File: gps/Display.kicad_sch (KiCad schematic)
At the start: 14 parts, among them U4 HT16k33, U5 7seg_1x1_rgb, U6 7seg_1x1_rgb, U7 7seg_1x1_rgb, U8 CA56-12CGKWA

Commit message: update pcd/sch
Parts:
- U8: footprint Display_7Segment:CA56-12CGKWA -> 7seg_rgb:7seg_4x1
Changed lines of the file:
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@@
 			)
 		)
-		(property "Footprint" "Display_7Segment:CA56-12CGKWA"
+		(property "Footprint" "7seg_rgb:7seg_4x1"
 			(at 128.27 114.3 0)
 			(effects

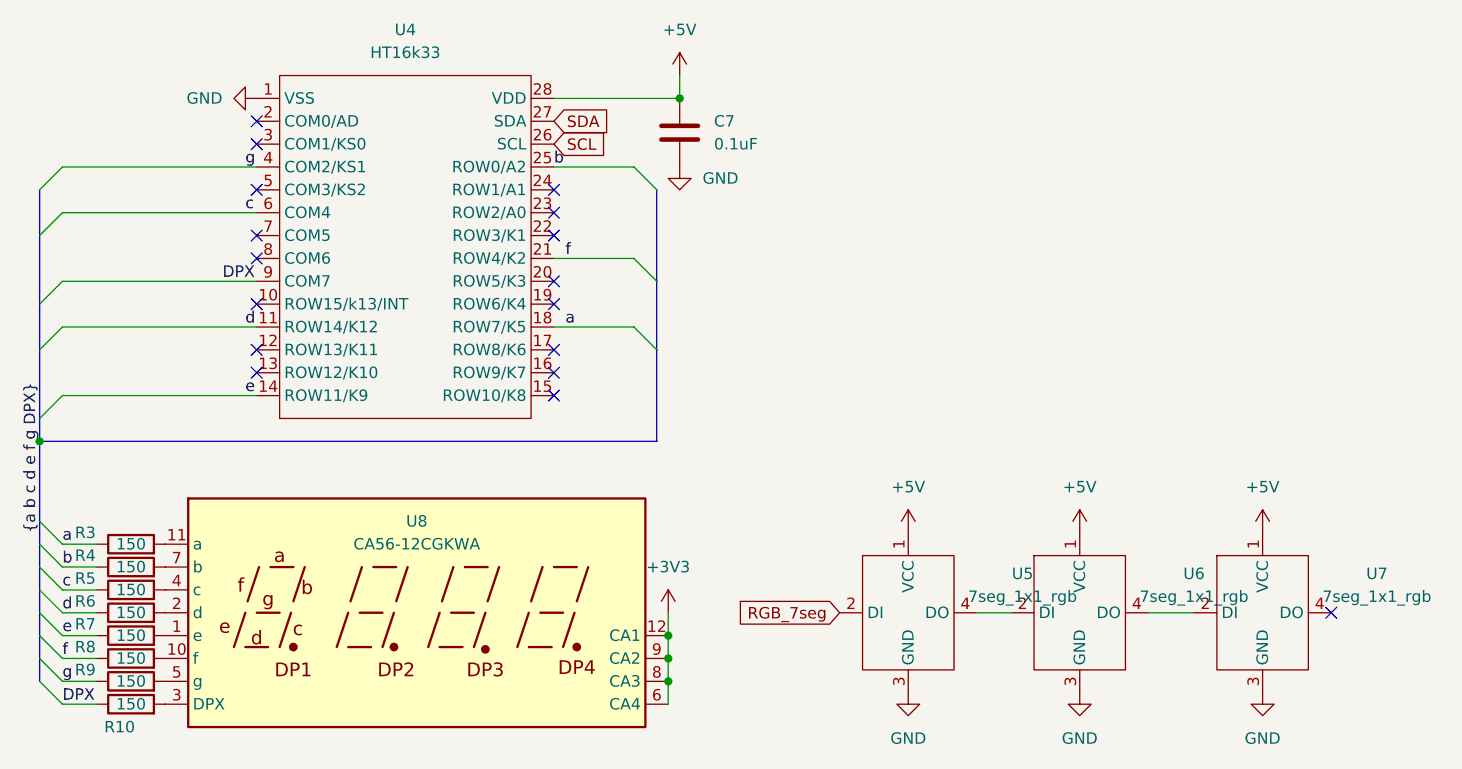
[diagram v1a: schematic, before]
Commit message: update pcd/sch
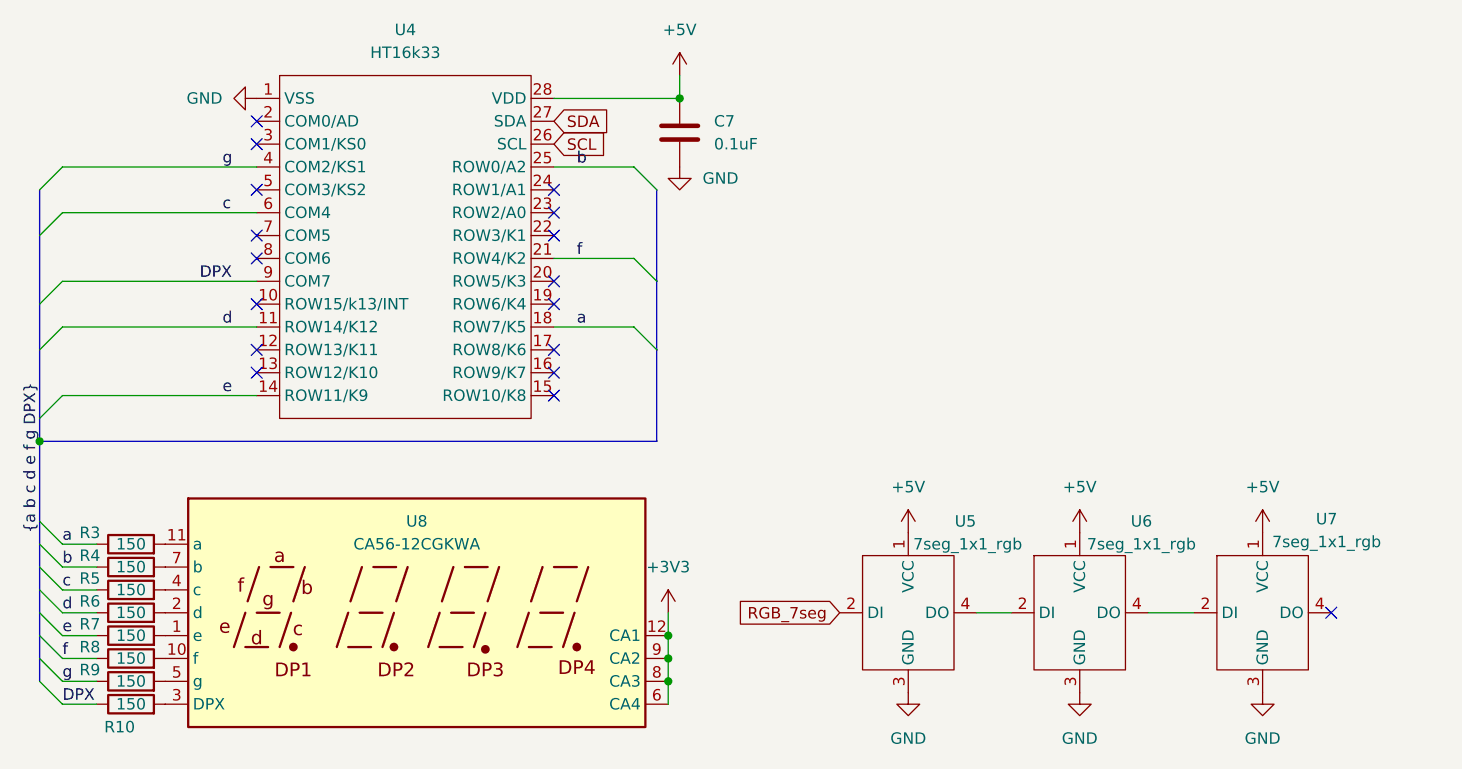
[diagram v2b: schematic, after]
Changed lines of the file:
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@@
+		)
+	)
+	(wire
+		(pts
+			(xy 143.51 49.53) (xy 152.4 49.53)
+		)
+		(stroke
+			(width 0)
+			(type default)
 		)
 	)
@@
 	(wire
 		(pts
-			(xy 152.4 49.53) (xy 143.51 49.53)
+			(xy 143.51 59.69) (xy 152.4 59.69)
 		)
 		(stroke
@@
 	(wire
 		(pts
-			(xy 143.51 59.69) (xy 152.4 59.69)
-		)
-		(stroke
-			(width 0)
-			(type default)
-		)
-	)
-	(wire
-		(pts
 			(xy 156.21 101.6) (xy 156.21 104.14)
 		)
@@
 	)
 	(label "DPX"
-		(at 106.68 62.23 0)
+		(at 104.14 62.23 0)
 		(fields_autoplaced yes)
 		(effects
@@
 	)
 	(label "e"
-		(at 109.22 74.93 0)
+		(at 106.68 74.93 0)
 		(fields_autoplaced yes)
 		(effects
@@
 	)
 	(label "a"
-		(at 144.78 67.31 0)
+		(at 146.05 67.31 0)
 		(fields_autoplaced yes)
 		(effects
@@
 	)
 	(label "g"
-		(at 109.22 49.53 0)
+		(at 106.68 49.53 0)
 		(fields_autoplaced yes)
 		(effects
@@
 	)
 	(label "d"
-		(at 109.22 67.31 0)
+		(at 106.68 67.31 0)
 		(fields_autoplaced yes)
 		(effects
@@
 	)
 	(label "f"
-		(at 144.78 59.69 0)
+		(at 146.05 59.69 0)
 		(fields_autoplaced yes)
 		(effects
@@
 	)
 	(label "b"
-		(at 143.51 49.53 0)
+		(at 146.05 49.53 0)
 		(fields_autoplaced yes)
 		(effects
@@
 	)
 	(label "c"
-		(at 109.22 54.61 0)
+		(at 106.68 54.61 0)
 		(fields_autoplaced yes)
 		(effects
@@
 		(dnp no)
 		(property "Reference" "R9"
-			(at 91.44 105.41 90)
+			(at 91.948 105.41 90)
 			(effects
 				(font
@@
 		(dnp no)
 		(property "Reference" "R6"
-			(at 91.44 97.79 90)
+			(at 91.948 97.79 90)
 			(effects
 				(font
@@
 		(dnp no)
 		(property "Reference" "R7"
-			(at 91.44 100.33 90)
+			(at 91.948 100.33 90)
 			(effects
 				(font
@@
 		(dnp no)
 		(property "Reference" "R5"
-			(at 91.44 95.25 90)
+			(at 91.948 95.25 90)
 			(effects
 				(font
@@
 		(dnp no)
 		(property "Reference" "R8"
-			(at 91.44 102.87 90)
+			(at 91.948 102.87 90)
 			(effects
 				(font
@@
 		(on_board yes)
 		(dnp no)
-		(fields_autoplaced yes)
 		(property "Reference" "U5"
-			(at 195.58 94.7293 0)
+			(at 189.23 88.9 0)
 			(effects
 				(font
@@
 		)
 		(property "Value" "7seg_1x1_rgb"
-			(at 195.58 97.2693 0)
+			(at 189.484 91.44 0)
 			(effects
 				(font
@@
 		(on_board yes)
 		(dnp no)
-		(fields_autoplaced yes)
 		(property "Reference" "U6"
-			(at 214.63 94.7293 0)
+			(at 208.788 88.9 0)
 			(effects
 				(font
@@
 		)
 		(property "Value" "7seg_1x1_rgb"
-			(at 214.63 97.2693 0)
+			(at 208.788 91.44 0)
 			(effects
 				(font
@@
 		(dnp no)
 		(property "Reference" "R3"
-			(at 91.44 90.17 90)
+			(at 91.948 90.17 90)
 			(effects
 				(font
@@
 		(dnp no)
 		(property "Reference" "R4"
-			(at 91.44 92.71 90)
+			(at 91.948 92.71 90)
 			(effects
 				(font
@@
 		(on_board yes)
 		(dnp no)
-		(fields_autoplaced yes)
 		(property "Reference" "U7"
-			(at 234.95 94.7293 0)
+			(at 229.362 88.646 0)
 			(effects
 				(font
@@
 		)
 		(property "Value" "7seg_1x1_rgb"
-			(at 234.95 97.2693 0)
-			(effects
-				(font
+			(at 229.362 91.186 0)
+			(effects
+				(font

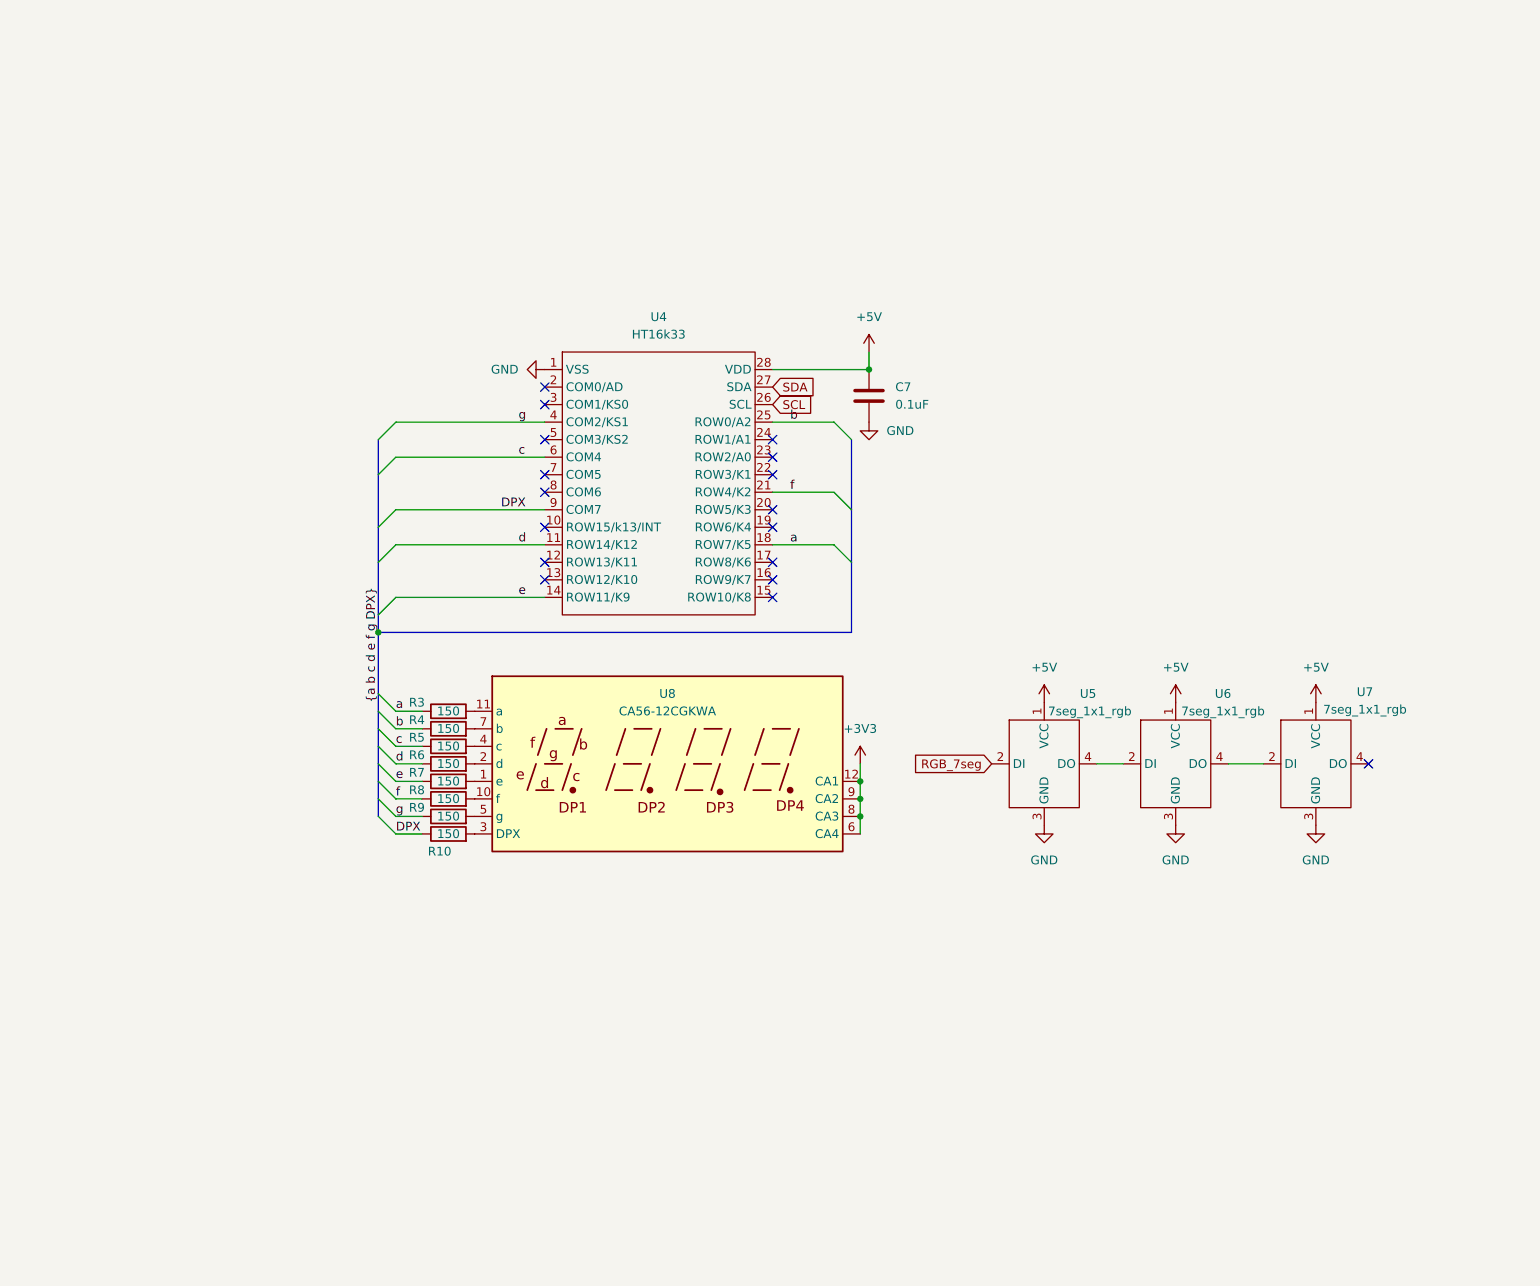
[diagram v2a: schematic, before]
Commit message: update pcb/housing
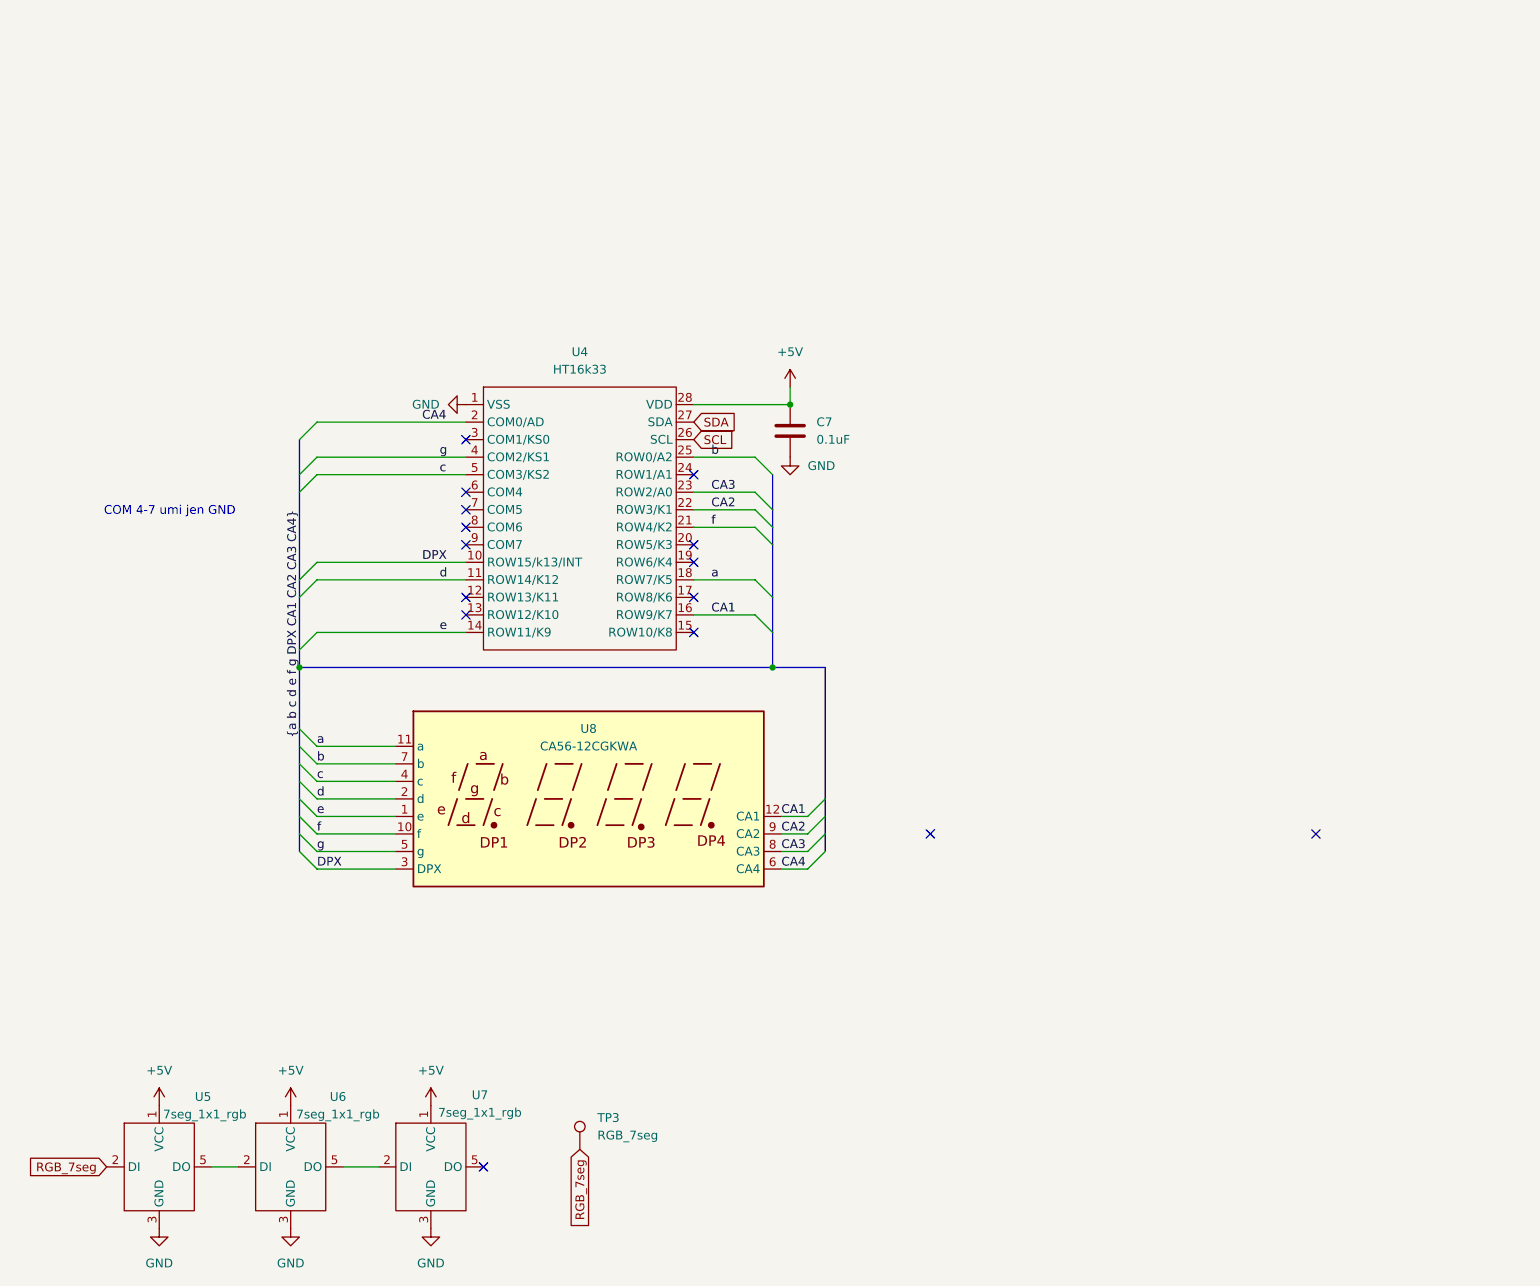
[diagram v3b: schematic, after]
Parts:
- removed R10, R3, R4, R5, R6, R7, R8, R9: 150, Resistor_SMD:R_0805_2012Metric_Pad1.20x1.40mm_HandSolder, symbol Device:R
- added TP3: RGB_7seg, TestPoint:TestPoint_Loop_D1.80mm_Drill1.0mm_Beaded, symbol Connector:TestPoint
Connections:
- net DPX: now also U4.10 (ROW15/k13/INT), U8.3 (DPX); no longer U4.9 (COM7)
- net RGB_7seg: now also TP3.1
- net a: now also U8.11 (a)
- net b: now also U8.7 (b)
- net c: now also U4.5 (COM3/KS2), U8.4 (c); no longer U4.6 (COM4)
- net d: now also U8.2 (d)
- net e: now also U8.1 (e)
- net f: now also U8.10 (f)
- net g: now also U8.5 (g)
- net CA1: now reaches U4.16 (ROW9/K7)
- net CA1: now also U8.12 (CA1)
- net CA4: now reaches U4.2 (COM0/AD)
- net CA4: now also U8.6 (CA4)
- net CA2: now reaches U4.22 (ROW3/K1)
- net CA2: now also U8.9 (CA2)
- net CA3: now reaches U4.23 (ROW2/A0)
- net CA3: now also U8.8 (CA3)
- net at U6.2 (DI): now also U5.5 (DO); no longer U5.4 (DO)
- net at U7.2 (DI): now also U6.5 (DO); no longer U6.4 (DO)
- removed net +3V3: U8.12 (CA1), U8.6 (CA4), U8.8 (CA3), U8.9 (CA2)
- no-connect marks 17 -> 15
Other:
- note added: "COM 4-7 umi jen GND"
- moved on the sheet: C7, U4, U5, U6, U7, U8

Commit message: update
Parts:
- added DS1: LTC-4724JF, Display_7Segment:LTC4724JF, symbol LTC-4724JF:LTC-4724JF
- C7: value 0.1uF -> 100nF; footprint Capacitor_SMD:C_0603_1608Metric_Pad1.08x0.95mm_HandSolder -> Capacitor_SMD:C_0805_2012Metric_Pad1.18x1.45mm_HandSolder
- U8: value CA56-12CGKWA -> KW4-804AGB
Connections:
- net CA4: now also U4.24 (ROW1/A1); no longer U4.2 (COM0/AD)
- net b: now also U4.4 (COM2/KS1); no longer U4.25 (ROW0/A2)
- net d: now also U4.8 (COM6); no longer U4.11 (ROW14/K12)
- net f: now also U4.3 (COM1/KS0); no longer U4.21 (ROW4/K2)
- net g: now also U4.5 (COM3/KS2); no longer U4.4 (COM2/KS1)
- net aBL2: now reaches U4.12 (ROW13/K11)
- net aBL2: now also DS1.11 (ANODE_BL2)
- net aAL1: now reaches U4.13 (ROW12/K10)
- net aAL1: now also DS1.12 (ANODE_AL1)
- net aE: now reaches U4.15 (ROW10/K8)
- net aE: now also DS1.2 (ANODE_E)
- net aCL3: now reaches U4.17 (ROW8/K6)
- net aCL3: now also DS1.3 (ANODE_CL3)
- net aD: now reaches U4.19 (ROW6/K4)
- net aD: now also DS1.4 (ANODE_D)
- net CC2: now reaches U4.6 (COM4)
- net CC2: now also U8.4 (c), DS1.5 (COMMON_CATHODE_DIGIT_2)
- net CC1: now reaches U4.7 (COM5)
- net CC1: now also U8.3 (DPX), DS1.1 (COMMON_CATHODE_DIGIT_1)
- net L123: now reaches U4.9 (COM7)
- net L123: now also U8.1 (e), DS1.14 (COMMON_CATHODE__L1L2L3)
- net DPX: no longer names the net of U4.10 (ROW15/k13/INT)
- net DPX: no longer U8.3 (DPX)
- net a: no longer names the net of U4.18 (ROW7/K5)
- net a: no longer U8.11 (a)
- removed net c: U4.5 (COM3/KS2), U8.4 (c)
- net e renamed aDP
- net aDP: now also DS1.6 (ANODE_DP); no longer U8.1 (e)
- new net CC3: DS1.7 (COMMON_CATHODE_DIGIT_3), U4.2 (COM0/AD), U8.11 (a)
- new net aF: DS1.15 (ANODE_F), U4.11 (ROW14/K12)
- new net aG: DS1.8 (ANODE_G), U4.25 (ROW0/A2)
- no-connect marks 15 -> 5
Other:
- note added: "ROW+ anode COM- cathode"

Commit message: PCB-update
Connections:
- net aAL1: now also U4.12 (ROW13/K11); no longer U4.13 (ROW12/K10)
- net aBL2: now also U4.13 (ROW12/K10); no longer U4.12 (ROW13/K11)
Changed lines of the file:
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@@
 	(generator_version "8.0")
 	(paper "A4")
+	(bus_alias "7Seg"
+		(members "a" "b" "c" "d" "e" "f" "g" "DPX" "CA1" "CA2" "CA3" "CA4" "CC1"
+			"CC2" "CC3" "L123" "aE" "aD" "aDP" "aCL3" "aF" "aAL1" "aBL2" "aG"
+		)
+	)
 	(junction
 		(at 74.93 85.09)
@@
 		)
 	)
-	(label "aAL1"
-		(at 92.71 77.47 0)
-		(fields_autoplaced yes)
-		(effects
-			(font
-				(size 1.27 1.27)
-			)
-			(justify left bottom)
-		)
-	)
 	(label "c"
 		(at 77.47 101.6 0)
@@
 		)
 	)
+	(label "{7Seg}"
+		(at 82.55 85.09 0)
+		(fields_autoplaced yes)
+		(effects
+			(font
+				(size 1.27 1.27)
+			)
+			(justify left bottom)
+		)
+	)
 	(label "CA1"
 		(at 144.78 106.68 0)
@@
 		)
 	)
+	(label "aAL1"
+		(at 92.71 74.93 0)
+		(fields_autoplaced yes)
+		(effects
+			(font
+				(size 1.27 1.27)
+			)
+			(justify left bottom)
+		)
+	)
 	(label "CA3"
 		(at 134.62 59.69 0)
@@
 		)
 	)
-	(label "aBL2"
-		(at 92.71 74.93 0)
-		(fields_autoplaced yes)
-		(effects
-			(font
-				(size 1.27 1.27)
-			)
-			(justify left bottom)
-		)
-	)
 	(label "aD"
 		(at 135.89 69.85 0)
@@
 		)
 	)
-	(label "{a b c d e f g DPX CA1 CA2 CA3 CA4 CC1 CC2 CC3 L123 aE aD aDP aCL3 aF aAL1 aBL2 aG }"
-		(at 74.93 95.25 90)
-		(fields_autoplaced yes)
-		(effects
-			(font
-				(size 1.27 1.27)
-			)
-			(justify left bottom)
-		)
-	)
 	(label "DPX"
 		(at 77.47 114.3 0)
@@
 		(fields_autoplaced yes)
 		(effects
+			(font
+				(size 1.27 1.27)
+			)
+			(justify left bottom)
+		)
+	)
+	(label "aBL2"
+		(at 92.71 77.47 0)
+		(fields_autoplaced yes)
+		(effects
